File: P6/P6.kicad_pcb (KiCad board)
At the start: 2 copper layers, 180.8 x 191.8 mm, 25 parts, among them J1 Conn_01x10, J2 Conn_01x10, SW13 SW_SPST, SW14 SW_SPST, SW15 SW_SPST, SW16 SW_SPST

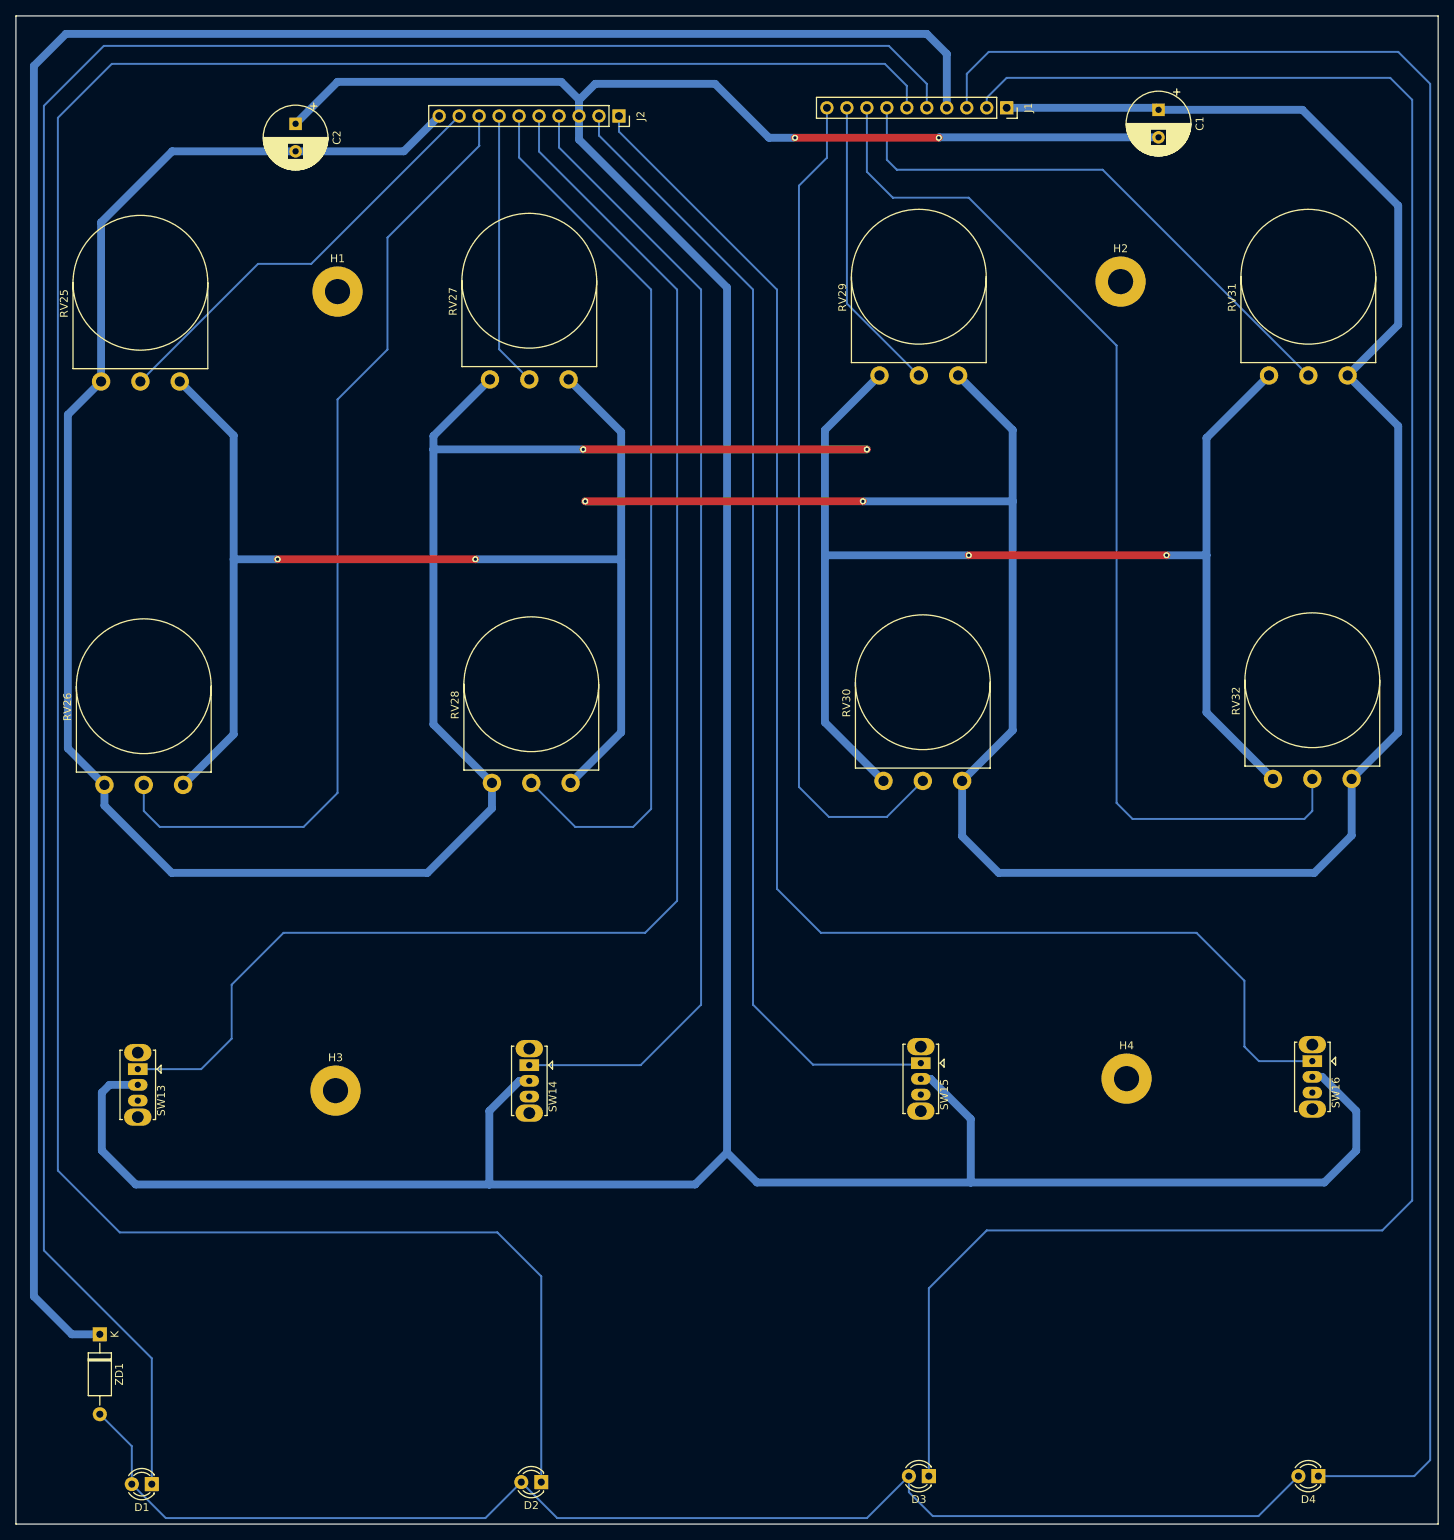
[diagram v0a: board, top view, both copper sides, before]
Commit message: Update footprints from library on P6
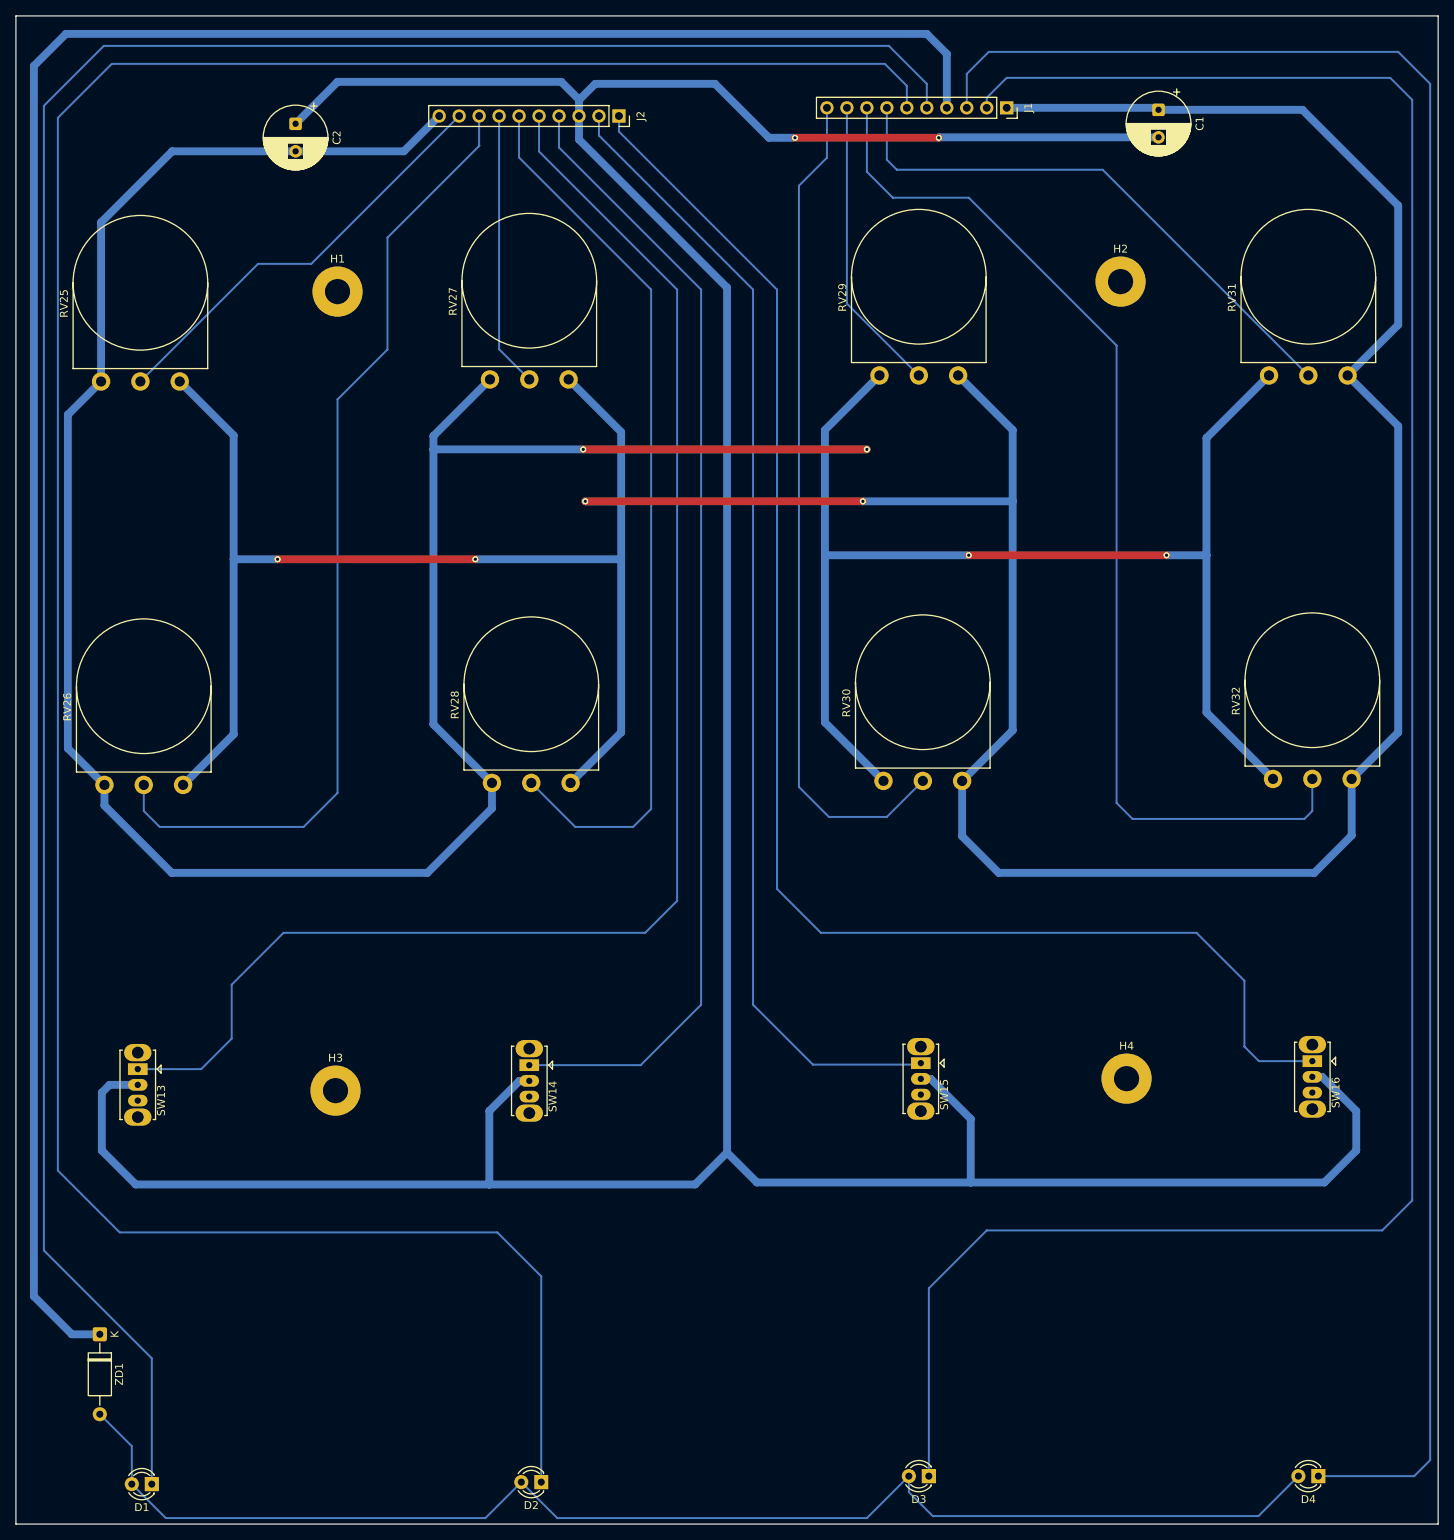
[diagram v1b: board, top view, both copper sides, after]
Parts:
- SW13, SW14, SW15, SW16: footprint Button_Switch_THT:SW_Slide_1P2T_CK_OS102011MS2Q -> Button_Switch_THT:SW_Slide_SPDT_Straight_CK_OS102011MS2Q
